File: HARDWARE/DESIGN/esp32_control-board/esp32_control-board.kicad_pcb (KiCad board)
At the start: 2 copper layers, 130 x 105 mm, 195 parts, among them J101 Power-in, J201 RFID-module1, J202 RFID-module2, J203 USB-Prog, J204 UART-Debug, J301 Lamp1, J302 Lamp2, J303 Lamp3, J304 Lamp4, J305 Lamp5, J306 Lamp6, J307 Lamp7, J308 Lamp8, J401 Lock1, J402 Lock2, J403 Lock3, J404 Lock4, J405 Lock5, J406 Lock6, J407 Lock7, J408 Lock8, Q102 DMP3013SFV-7, Q201 SS8050, Q202 SS8050, SW201 Boot, SW202 Reset, U101 LM63615DQDRRRQ1, U102 AMS1117-3.3, U201 CH343P, U202 USBLC6-2SC6, U203 ESP32-S3-WROOM-1, U204 USBLC6-2SC6, U301 MCP23008-xSS, U302 TBD62783A, U303 TBD62783A, U401 PC817, U402 PC817, U403 PC817, U404 PC817, U405 PC817, U406 PC817, U407 PC817, U408 PC817

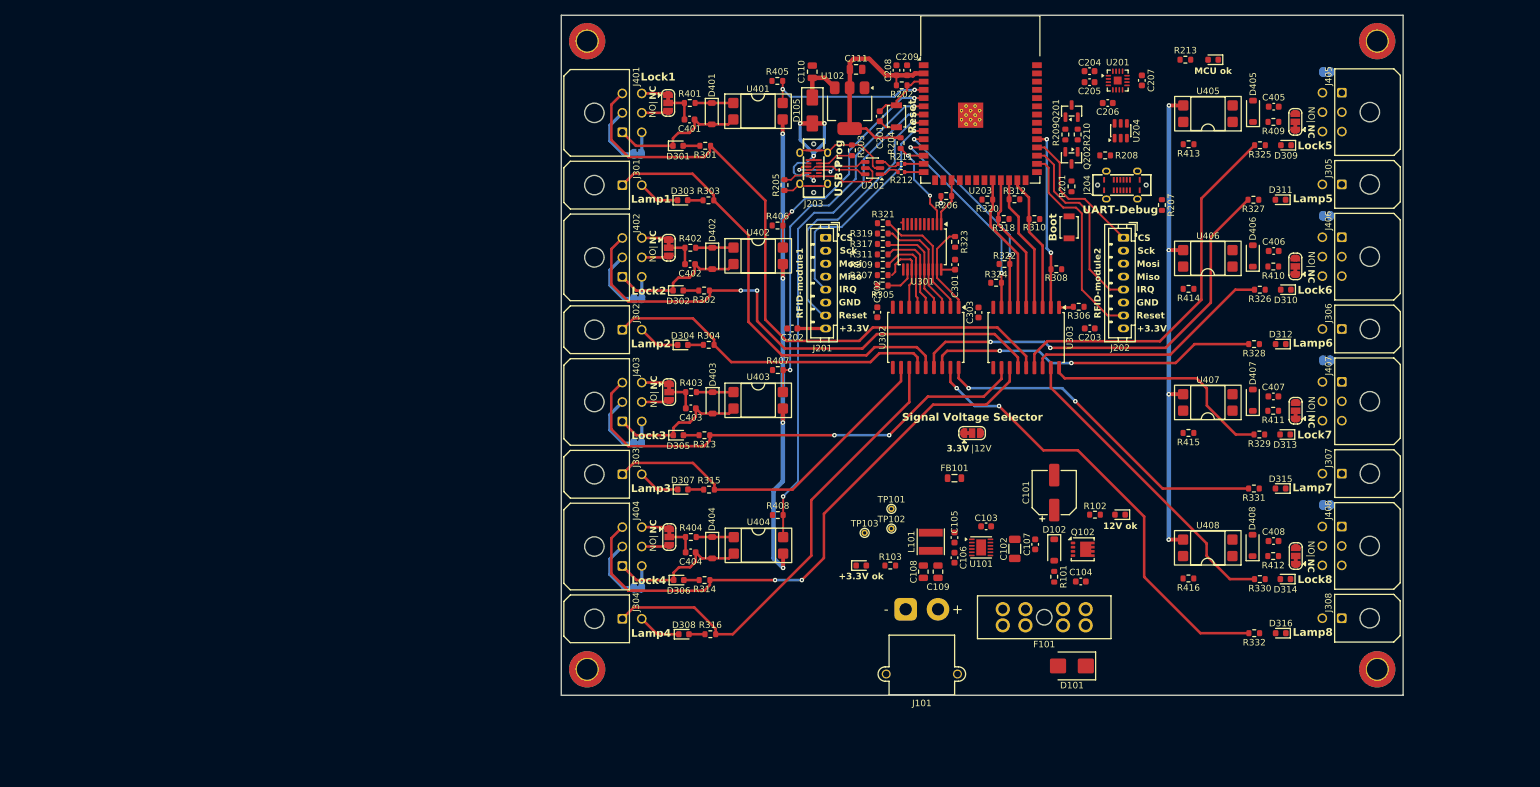
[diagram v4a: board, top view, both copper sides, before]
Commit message: 60715 - traced 75%
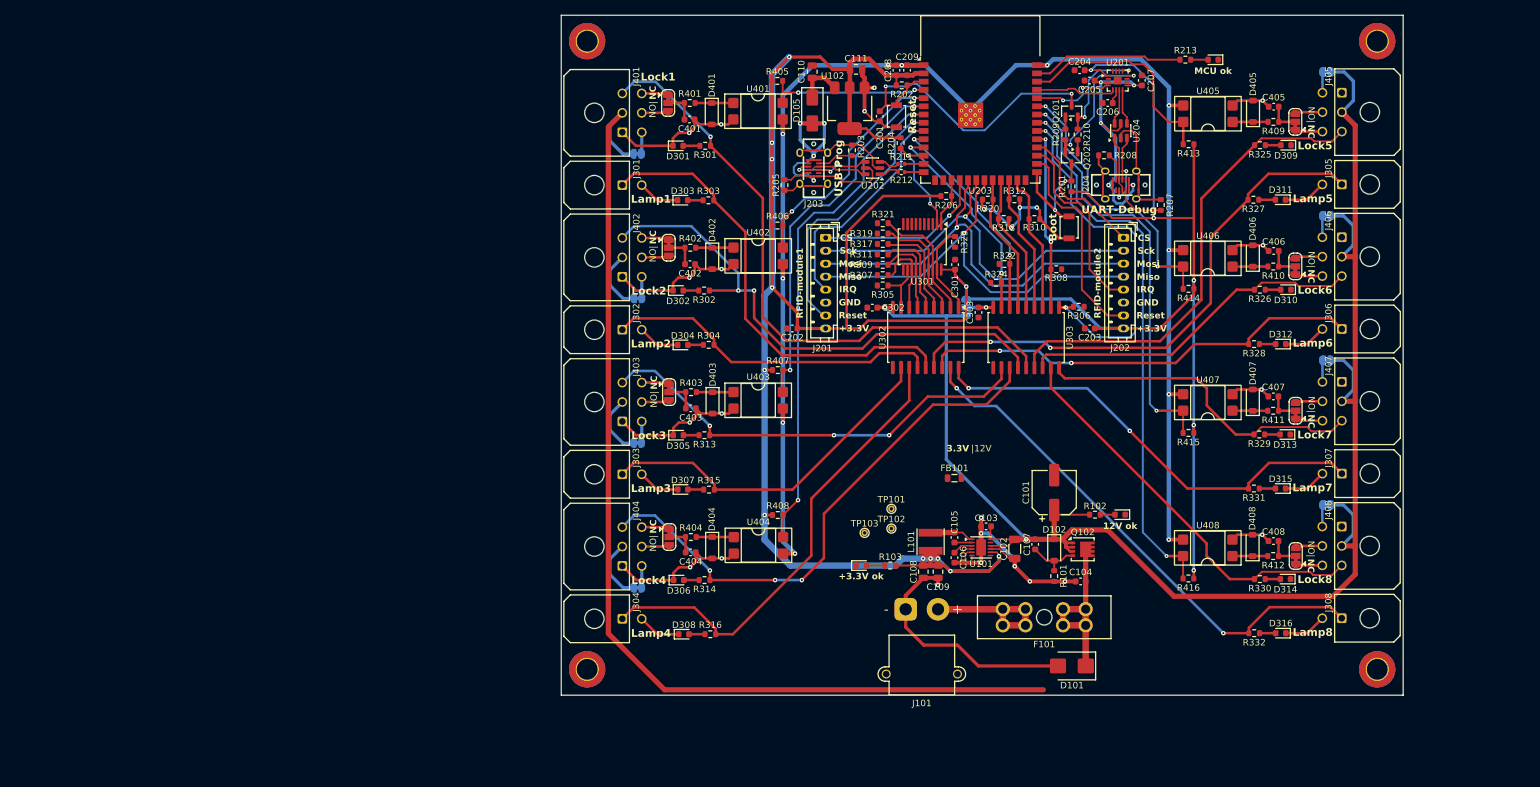
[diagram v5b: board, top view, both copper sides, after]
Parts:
- JP301: moved to B.Cu
- moved JP301 19.4 mm to (132.8, 95.0), turned to -90 degrees
- moved C204 1.54 mm to (150.3, 58.4)
- moved C302 1.05 mm to (118.3, 95.1), turned to 0 degrees
- moved C205 0.25 mm to (151.8, 60.0)
- moved J204 0.17 mm to (156.7, 76.1)
- moved R208 0.17 mm to (154.1, 71.5)
- moved R207 0.17 mm to (162.8, 79.2)
- moved R101 0.10 mm to (146.4, 136.5)
- moved R320 0.07 mm to (136.1, 78.4)
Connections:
- C208 pad 1: GND -> GND_MCU
- C209 pad 1: GND -> GND_MCU
- D201 pad 1: GND -> GND_MCU
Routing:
- net +3V3: track 40.6 -> 476.5 mm, vias 1 -> 17
- net +12V: track 38.3 -> 446.5 mm, vias 0 -> 2
- net GND: track 139.5 -> 335.4 mm, vias 0 -> 25
- net LOCK8_signal: track 0.00 -> 85.0 mm, vias 0 -> 2
- net GND_MCU: track 153.0 -> 231.2 mm, vias 8 -> 11
- net SPI_miso: track 0.00 -> 66.0 mm, vias 0 -> 1
- net SPI_mosi: track 0.00 -> 64.9 mm, vias 0 -> 1
- net LOCK7_signal: track 0.00 -> 64.7 mm, vias 0 -> 2
- net SPI_sck: track 0.00 -> 63.3 mm, vias 0 -> 1
- net LOCK1_do: track 2.25 -> 56.3 mm, vias 0 -> 2
- net Vusb: track 38.9 -> 82.8 mm, vias 4 -> 9
- net LOCK6_signal: track 0.00 -> 43.6 mm, vias 0 -> 2
- net esp_Reset: track 9.52 -> 48.4 mm, vias 0 -> 2
- net LOCK5_signal: track 0.00 -> 34.3 mm
- net +12V-fused: track 0.00 -> 27.5 mm
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
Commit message: 60825 - Schematic update and PCB-layout started
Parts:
- removed C203: 1u, Capacitor_SMD:C_0603_1608Metric
- removed C204, C205, C206, C207, C301, C302, C303: 100n, Capacitor_SMD:C_0603_1608Metric
- removed C401, C402, C403, C404, C405, C406, C407, C408: 1n, Capacitor_SMD:C_0603_1608Metric
- removed D301, D302, D305, D306, D309, D310, D313, D314: LOCK on, LED_SMD:LED_0603_1608Metric
- removed D303, D304, D307, D308, D311, D312, D315, D316: LAMP on, LED_SMD:LED_0603_1608Metric
- removed D401, D402, D403, D404, D405, D406, D407, D408: 1N4148W, Diode_SMD:D_SOD-123
- removed FB101: 80Ω@100MHz, Inductor_SMD:L_0805_2012Metric
- removed J202: RFID-module2, Connector_JST:JST_PH_B8B-PH-K_1x08_P2.00mm_Vertical
- removed J203: USB-Prog, (FOOTPRINTS):C3151749_USB_TYPE-C_Vertical
- removed J301: Lamp1, Connector_Molex:Molex_Micro-Fit_3.0_43045-0200_2x01_P3.00mm_Horizontal
- removed J302: Lamp2, Connector_Molex:Molex_Micro-Fit_3.0_43045-0200_2x01_P3.00mm_Horizontal
- removed J303: Lamp3, Connector_Molex:Molex_Micro-Fit_3.0_43045-0200_2x01_P3.00mm_Horizontal
- removed J304: Lamp4, Connector_Molex:Molex_Micro-Fit_3.0_43045-0200_2x01_P3.00mm_Horizontal
- removed J305: Lamp5, Connector_Molex:Molex_Micro-Fit_3.0_43045-0200_2x01_P3.00mm_Horizontal
- removed J306: Lamp6, Connector_Molex:Molex_Micro-Fit_3.0_43045-0200_2x01_P3.00mm_Horizontal
- removed J307: Lamp7, Connector_Molex:Molex_Micro-Fit_3.0_43045-0200_2x01_P3.00mm_Horizontal
- removed J308: Lamp8, Connector_Molex:Molex_Micro-Fit_3.0_43045-0200_2x01_P3.00mm_Horizontal
- removed J404: Lock4, Connector_Molex:Molex_Micro-Fit_3.0_43045-0600_2x03_P3.00mm_Horizontal
- removed JP301: Signal Voltage Selector, Jumper:SolderJumper-3_P1.3mm_Bridged12_RoundedPad1.0x1.5mm
- removed JP401, JP402, JP403, JP404, JP405, JP406, JP407, JP408: Switch State Selector, Jumper:SolderJumper-3_P1.3mm_Bridged12_RoundedPad1.0x1.5mm
- removed JP409, JP410, JP411, JP412, JP413, JP414, JP415, JP416: 12V-to-COM, Jumper:SolderJumper-2_P1.3mm_Bridged_RoundedPad1.0x1.5mm
- removed Q201, Q202: SS8050, Package_TO_SOT_SMD:SOT-23
- removed R101, R201, R202, R209, R210, R305, R306, R307, R308, R309, R310, R311, R312, R317, R318, R319, R320, R321, R322, R323, R324: 12k, Resistor_SMD:R_0603_1608Metric
- removed R203, R205, R301, R302, R303, R304, R313, R314, R315, R316, R325, R326, R327, R328, R329, R330, R331, R332: 5k1, Resistor_SMD:R_0603_1608Metric
- removed R401, R402, R403, R404, R409, R410, R411, R412: 1k2, Resistor_SMD:R_0603_1608Metric
- removed R405, R406, R407, R408, R413, R414, R415, R416: 10k, Resistor_SMD:R_0603_1608Metric
- removed U201: CH343P, Package_DFN_QFN:TQFN-16-1EP_3x3mm_P0.5mm_EP1.23x1.23mm
- removed U202: USBLC6-2SC6, Package_TO_SOT_SMD:SOT-23-6
- removed U301: MCP23008-xSS, Package_SO:SSOP-20_5.3x7.2mm_P0.65mm
- removed U302, U303: TBD62783A, Package_SO:SOIC-18W_7.5x11.6mm_P1.27mm
- removed U401, U402, U403, U404, U405, U406, U407, U408: PC817, Package_DIP:DIP-4_W7.62mm_SMDSocket_SmallPads
- added C210: 100n, Capacitor_SMD:C_0603_1608Metric, F.Cu at (48.5, 125.7)
- added C211: 100n, Capacitor_SMD:C_0603_1608Metric, F.Cu at (-3.02, 130.4)
- added C212: 10n, Capacitor_SMD:C_0603_1608Metric, F.Cu at (-3.02, 132.9)
- added C213: 10n, Capacitor_SMD:C_0603_1608Metric, F.Cu at (-3.02, 135.5)
- added C214: 10n, Capacitor_SMD:C_0603_1608Metric, F.Cu at (-3.02, 138.0)
- added C215: 10n, Capacitor_SMD:C_0603_1608Metric, F.Cu at (-3.02, 140.5)
- added C216: 100n, Capacitor_SMD:C_0603_1608Metric, F.Cu at (28.0, 150.7)
- added C217: 1u, Capacitor_SMD:C_0603_1608Metric, F.Cu at (48.5, 128.2)
- added C218: 4u7, Capacitor_SMD:C_0805_2012Metric, F.Cu at (13.2, 154.8)
- added C219: 4u7, Capacitor_SMD:C_0805_2012Metric, F.Cu at (13.2, 157.8)
- added C220: 10n, Capacitor_SMD:C_0603_1608Metric, F.Cu at (-3.02, 143.0)
- added C221: 10n, Capacitor_SMD:C_0603_1608Metric, F.Cu at (-3.02, 145.5)
- added C409: 1n, Capacitor_SMD:C_0603_1608Metric, F.Cu at (13.9, 105.8)
- added C410: 1n, Capacitor_SMD:C_0603_1608Metric, F.Cu at (13.9, 108.4)
- added C411: 1n, Capacitor_SMD:C_0603_1608Metric, F.Cu at (13.9, 110.9)
- added C412: 1n, Capacitor_SMD:C_0603_1608Metric, F.Cu at (13.9, 113.4)
- added D106: XL-1608UOC-06, LED_SMD:LED_0603_1608Metric, F.Cu at (2.28, 110.6)
- added D107: XL-1608UOC-06, LED_SMD:LED_0603_1608Metric, F.Cu at (2.28, 113.2)
- added D108: XL-1608UOC-06, LED_SMD:LED_0603_1608Metric, F.Cu at (2.28, 115.8)
- added D109: XL-1608UOC-06, LED_SMD:LED_0603_1608Metric, F.Cu at (2.28, 118.4)
- added D112: XL-1608UWC-04, LED_SMD:LED_0603_1608Metric, F.Cu at (8.97, 154.6)
- added D113: XL-1608UWC-04, LED_SMD:LED_0603_1608Metric, F.Cu at (8.97, 157.2)
- added D114: XL-1608UWC-04, LED_SMD:LED_0603_1608Metric, F.Cu at (8.97, 159.8)
- added D115: XL-1608UWC-04, LED_SMD:LED_0603_1608Metric, F.Cu at (8.97, 162.4)
- added D202: MCU ok, LED_SMD:LED_0603_1608Metric, F.Cu at (48.6, 135.8)
- added D203: XL-1608UBC-06A, LED_SMD:LED_0603_1608Metric, F.Cu at (48.6, 138.4)
- added D204: XL-1608SURUGC, LED_SMD:LED_0603_1608Metric, F.Cu at (48.6, 141.0)
- added D317: LAMP on, LED_SMD:LED_0603_1608Metric, F.Cu at (8.97, 165.0)
- added D409: 1N4148W, Diode_SMD:D_SOD-123, F.Cu at (19.8, 84.0)
- added D410: 1N4148W, Diode_SMD:D_SOD-123, F.Cu at (19.8, 87.4)
- added D411: 1N4148W, Diode_SMD:D_SOD-123, F.Cu at (19.8, 90.7)
- added D412: 1N4148W, Diode_SMD:D_SOD-123, F.Cu at (19.8, 94.1)
- added D5: PESD1CAN, Package_TO_SOT_SMD:SOT-23, F.Cu at (37.6, 165.4)
- added J309: Lamp1, Connector_Molex:Molex_Micro-Fit_3.0_43045-0200_2x01_P3.00mm_Horizontal, F.Cu at (11.6, 136.6)
- added J4: Termination, Connector_PinHeader_2.54mm:PinHeader_1x02_P2.54mm_Horizontal, F.Cu at (87.0, 61.4)
- added J409: Lock1, Connector_Molex:Molex_Micro-Fit_3.0_43045-0600_2x03_P3.00mm_Horizontal, F.Cu at (115.2, 145.9)
- added J410: Lock2, Connector_Molex:Molex_Micro-Fit_3.0_43045-0600_2x03_P3.00mm_Horizontal, F.Cu at (130.8, 145.8)
- added J411: B3B-PH-K-S(LF)(SN), Connector_JST:JST_PH_B3B-PH-K_1x03_P2.00mm_Vertical, F.Cu at (-12.0, 155.6)
- added J412: B3B-PH-K-S(LF)(SN), Connector_JST:JST_PH_B3B-PH-K_1x03_P2.00mm_Vertical, F.Cu at (-12.0, 162.2)
- added Q401: AO3401A, Package_TO_SOT_SMD:SOT-23, F.Cu at (14.4, 84.6)
- added Q402: BSS138, Package_TO_SOT_SMD:SOT-23, F.Cu at (14.4, 89.0)
- added Q403: BSS138, Package_TO_SOT_SMD:SOT-23, F.Cu at (14.4, 93.5)
- added Q404: AO3401A, Package_TO_SOT_SMD:SOT-23, F.Cu at (14.4, 97.9)
- added Q405: BSS138, Package_TO_SOT_SMD:SOT-23, F.Cu at (14.4, 102.4)
- added Q406: DMP6180SK3-13, Package_TO_SOT_SMD:TO-252-2, F.Cu at (-8.06, 116.0)
- added R105: 12k, Resistor_SMD:R_0603_1608Metric, F.Cu at (13.9, 115.9)
- added R106: 27k, Resistor_SMD:R_0603_1608Metric, F.Cu at (13.9, 118.4)
- added R107: 12k, Resistor_SMD:R_0603_1608Metric, F.Cu at (13.9, 120.9)
- added R108: 12k, Resistor_SMD:R_0603_1608Metric, F.Cu at (28.0, 109.2)
- added R109: 12k, Resistor_SMD:R_0603_1608Metric, F.Cu at (48.5, 130.7)
- added R110: 12k, Resistor_SMD:R_0603_1608Metric, F.Cu at (52.5, 120.7)
- added R111: 120, Resistor_SMD:R_0603_1608Metric, F.Cu at (13.9, 123.4)
- added R112: 120, Resistor_SMD:R_0603_1608Metric, F.Cu at (18.0, 105.8)
- added R113: 12k, Resistor_SMD:R_0603_1608Metric, F.Cu at (18.0, 108.4)
- added R114: 27k, Resistor_SMD:R_0603_1608Metric, F.Cu at (18.0, 110.9)
- added R115: 12k, Resistor_SMD:R_0603_1608Metric, F.Cu at (18.0, 113.4)
- added R116: 12k, Resistor_SMD:R_0603_1608Metric, F.Cu at (18.0, 115.9)
- added R117: 12k, Resistor_SMD:R_0603_1608Metric, F.Cu at (18.0, 118.4)
- added R118: 12k, Resistor_SMD:R_0603_1608Metric, F.Cu at (18.0, 120.9)
- added R119: 12k, Resistor_SMD:R_0603_1608Metric, F.Cu at (18.0, 123.4)
- added R120: 1M, Resistor_SMD:R_0603_1608Metric, F.Cu at (52.5, 123.2)
- added R121: 270k, Resistor_SMD:R_0603_1608Metric, F.Cu at (52.5, 125.7)
- added R122: 120, Resistor_SMD:R_0603_1608Metric, F.Cu at (28.0, 153.2)
- added R123: 12k, Resistor_SMD:R_0603_1608Metric, F.Cu at (28.0, 155.7)
- added R124: 120, Resistor_SMD:R_0603_1608Metric, F.Cu at (22.0, 105.8)
- added R125: 12k, Resistor_SMD:R_0603_1608Metric, F.Cu at (0.99, 127.9)
- added R126: 120, Resistor_SMD:R_0603_1608Metric, F.Cu at (0.99, 130.4)
- added R127: 12k, Resistor_SMD:R_0603_1608Metric, F.Cu at (0.99, 132.9)
- added R128: 120, Resistor_SMD:R_0603_1608Metric, F.Cu at (0.99, 135.5)
- added R129: 12k, Resistor_SMD:R_0603_1608Metric, F.Cu at (0.99, 138.0)
- added R130: 12k, Resistor_SMD:R_0603_1608Metric, F.Cu at (0.99, 140.5)
- added R131: 120, Resistor_SMD:R_0603_1608Metric, F.Cu at (0.99, 143.0)
- added R132: 120, Resistor_SMD:R_0603_1608Metric, F.Cu at (0.99, 145.5)
- added R133: 12k, Resistor_SMD:R_0603_1608Metric, F.Cu at (22.0, 108.4)
- added R134: 12k, Resistor_SMD:R_0603_1608Metric, F.Cu at (22.0, 110.9)
- added R214: 1k, Resistor_SMD:R_0603_1608Metric, F.Cu at (56.5, 128.2)
- added R215: 0R, Resistor_SMD:R_0402_1005Metric, F.Cu at (57.2, 108.6)
- added R333: 5k1, Resistor_SMD:R_0603_1608Metric, F.Cu at (5.00, 127.9)
- added R417: 1k, Resistor_SMD:R_0603_1608Metric, F.Cu at (22.0, 113.4)
- added R419: 1k, Resistor_SMD:R_0603_1608Metric, F.Cu at (22.0, 115.9)
- added R420: 1k, Resistor_SMD:R_0603_1608Metric, F.Cu at (22.0, 118.4)
- added R421: 1k, Resistor_SMD:R_0603_1608Metric, F.Cu at (22.0, 120.9)
- added R422: 1k, Resistor_SMD:R_0603_1608Metric, F.Cu at (5.00, 130.4)
- added R423: 1k, Resistor_SMD:R_0603_1608Metric, F.Cu at (5.00, 132.9)
- added R424: 1k, Resistor_SMD:R_0603_1608Metric, F.Cu at (5.00, 135.5)
- added R425: 1k, Resistor_SMD:R_0603_1608Metric, F.Cu at (5.00, 138.0)
- added R426: 1k, Resistor_SMD:R_0603_1608Metric, F.Cu at (5.00, 140.5)
- added R427: 1k, Resistor_SMD:R_0603_1608Metric, F.Cu at (5.00, 143.0)
- added U205: USBLC6-2SC6, Package_TO_SOT_SMD:SOT-23-6, F.Cu at (13.6, 161.7)
- added U409: PC817, Package_DIP:DIP-4_W7.62mm_SMDSocket_SmallPads, F.Cu at (6.09, 85.7)
- added U410: PC817, Package_DIP:DIP-4_W7.62mm_SMDSocket_SmallPads, F.Cu at (6.09, 92.5)
- added U411: PC817, Package_DIP:DIP-4_W7.62mm_SMDSocket_SmallPads, F.Cu at (6.09, 99.2)
- added U412: PC817, Package_DIP:DIP-4_W7.62mm_SMDSocket_SmallPads, F.Cu at (6.09, 106.0)
- added U6: TCAN330, Package_TO_SOT_SMD:SOT-23-8, F.Cu at (32.6, 165.5)
- C208: value 1u -> 22u; footprint Capacitor_SMD:C_0603_1608Metric -> Capacitor_SMD:C_0805_2012Metric
- J204: value UART-Debug -> USB-prog
- J401: value Lock1 -> B3B-PH-K-K(LF)(SN); footprint Connector_Molex:Molex_Micro-Fit_3.0_43045-0600_2x03_P3.00mm_Horizontal -> Connector_JST:JST_PH_B3B-PH-K_1x03_P2.00mm_Vertical
- J402: value Lock2 -> B4B-PH-K-S(LF)(SN); footprint Connector_Molex:Molex_Micro-Fit_3.0_43045-0600_2x03_P3.00mm_Horizontal -> Connector_JST:JST_PH_B4B-PH-K_1x04_P2.00mm_Vertical
- J403: value Lock3 -> B4B-PH-K-S(LF)(SN); footprint Connector_Molex:Molex_Micro-Fit_3.0_43045-0600_2x03_P3.00mm_Horizontal -> Connector_JST:JST_PH_B4B-PH-K_1x04_P2.00mm_Vertical
- J405: value Lock5 -> B3B-PH-K-S(LF)(SN); footprint Connector_Molex:Molex_Micro-Fit_3.0_43045-0600_2x03_P3.00mm_Horizontal -> Connector_JST:JST_PH_B3B-PH-K_1x03_P2.00mm_Vertical
- J406: value Lock6 -> B3B-PH-K-S(LF)(SN); footprint Connector_Molex:Molex_Micro-Fit_3.0_43045-0600_2x03_P3.00mm_Horizontal -> Connector_JST:JST_PH_B3B-PH-K_1x03_P2.00mm_Vertical
- J407: value Lock7 -> B3B-PH-K-S(LF)(SN); footprint Connector_Molex:Molex_Micro-Fit_3.0_43045-0600_2x03_P3.00mm_Horizontal -> Connector_JST:JST_PH_B3B-PH-K_1x03_P2.00mm_Vertical
- J408: value Lock8 -> B3B-PH-K-S(LF)(SN); footprint Connector_Molex:Molex_Micro-Fit_3.0_43045-0600_2x03_P3.00mm_Horizontal -> Connector_JST:JST_PH_B3B-PH-K_1x03_P2.00mm_Vertical
- U203: value ESP32-S3-WROOM-1 -> ESP32-S3-WROOM-1U; footprint RF_Module:ESP32-S3-WROOM-1 -> RF_Module:ESP32-S3-WROOM-1U
- moved J405 213.7 mm to (-12.0, 129.4), turned to 0 degrees
- moved J406 209.3 mm to (-12.0, 135.9), turned to 0 degrees
- moved J407 206.0 mm to (-12.0, 142.5), turned to 0 degrees
- moved J408 203.8 mm to (-12.0, 149.1), turned to 0 degrees
- moved D201 144.3 mm to (48.6, 133.2), turned to 0 degrees
- moved R213 129.9 mm to (56.5, 125.7)
- moved C104 129.9 mm to (28.0, 94.2)
- moved R102 126.8 mm to (28.0, 104.2), turned to 0 degrees
- moved C107 119.3 mm to (28.0, 101.7), turned to 0 degrees
- moved C103 114.1 mm to (28.0, 91.7), turned to 0 degrees
- moved R207 114.1 mm to (56.5, 120.7), turned to 0 degrees
- moved C202 112.9 mm to (-3.02, 127.9), turned to 0 degrees
- moved R208 110.3 mm to (56.5, 123.2)
- moved C208 108.6 mm to (52.8, 142.2), turned to 0 degrees
- moved C106 108.6 mm to (28.0, 99.2), turned to 0 degrees
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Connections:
- net esp_LED renamed esp_LED_green
- J204 pad A6: espS_USB_dp -> esp_USB_dP
- J204 pad A7: espS_USB_dm -> esp_USB_dN
- J204 pad B6: espS_USB_dp -> esp_USB_dP
- J204 pad B7: espS_USB_dm -> esp_USB_dN
- J401 pad 1: GND -> CAN+_conn.
- J401 pad 2: +12V -> CAN-_conn.
- J401 pad 3: LOCK1_ctrl -> GND
- J402 pad 1: GND -> +3V3
- J402 pad 2: +12V -> GND
- J402 pad 3: LOCK2_ctrl -> I2C_sda
- J402 pad 4: SWITCH2-COM -> I2C_scl
- J403 pad 1: GND -> +3V3
- J403 pad 2: +12V -> GND
- J403 pad 3: LOCK3_ctrl -> esp_TXD
- J403 pad 4: SWITCH3-COM -> esp_RXD
- J405 pad 1: GND -> +3V3
- J405 pad 2: +12V -> GND
- J405 pad 3: LOCK5_ctrl -> di_SENSOR_ext1
- J406 pad 1: GND -> +3V3
- J406 pad 2: +12V -> GND
- J406 pad 3: LOCK6_ctrl -> di_SENSOR_ext2
- J407 pad 1: GND -> +3V3
- J407 pad 2: +12V -> GND
- J407 pad 3: LOCK7_ctrl -> di_SENSOR_ext3
- J408 pad 1: GND -> +3V3
- J408 pad 2: +12V -> GND
- J408 pad 3: LOCK8_ctrl -> di_SENSOR_ext4
- R211 pad 1: espU_USB_d- -> esp_USB_d-
- R212 pad 1: espU_USB_d+ -> esp_USB_d+
- U203 pad 10: LOCK7_do -> unconnected-(U203-IO17-Pad10)
- U203 pad 11: LOCK8_do -> unconnected-(U203-IO18-Pad11)
- U203 pad 22: LOCK6_do -> unconnected-(U203-IO14-Pad22)
- U203 pad 23: LOCK5_do -> unconnected-(U203-IO21-Pad23)
- U203 pad 24: LOCK4_do -> unconnected-(U203-IO47-Pad24)
- U203 pad 25: LOCK3_do -> unconnected-(U203-IO48-Pad25)
- U203 pad 28: RFID2_reset -> unconnected-(U203-IO35-Pad28)
- U203 pad 29: RFID2_irq -> unconnected-(U203-IO36-Pad29)
- U203 pad 30: SPI_cs2 -> unconnected-(U203-IO37-Pad30)
- U203 pad 31: LOCK2_do -> unconnected-(U203-IO38-Pad31)
- U203 pad 32: LOCK1_do -> unconnected-(U203-IO39-Pad32)
- U203 pad 33: LOCK8_signal -> unconnected-(U203-IO40-Pad33)
- U203 pad 34: LOCK7_signal -> unconnected-(U203-IO41-Pad34)
- U203 pad 35: LOCK6_signal -> unconnected-(U203-IO42-Pad35)
- U203 pad 38: LOCK5_signal -> unconnected-(U203-IO2-Pad38)
- U203 pad 4: LOCK1_signal -> TWAI_TX
- U203 pad 5: LOCK2_signal -> TWAI_RX
- U203 pad 6: LOCK3_signal -> esp_ADC1_ch5
- U203 pad 7: LOCK4_signal -> esp_ADC1_ch6
- U204 pad 1: espS_USB_dp -> esp_USB_dN
- U204 pad 3: espS_USB_dm -> esp_USB_dP
- U204 pad 4: espS_USB_d- -> esp_USB_d+
- U204 pad 6: espS_USB_d+ -> esp_USB_d-
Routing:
- net +3V3: track 476.5 -> 0.00 mm, vias 17 -> 0
- net +12V: track 446.5 -> 0.00 mm, vias 2 -> 0
- net GND: track 335.4 -> 0.00 mm, vias 25 -> 0
- net GND_MCU: track 231.2 -> 0.00 mm, vias 11 -> 0
- net LOCK1_ctrl: track 95.7 -> 0.00 mm, vias 1 -> 0
- net LOCK8_signal: track 85.0 -> 0.00 mm, vias 2 -> 0
- net LAMP5: track 84.6 -> 0.00 mm, vias 2 -> 0
- net LOCK4_ctrl: track 84.4 -> 0.00 mm, vias 3 -> 0
- net Vusb: track 82.8 -> 0.00 mm, vias 9 -> 0
- net LOCK2_ctrl: track 82.2 -> 0.00 mm, vias 2 -> 0
- net LAMP8: track 81.6 -> 0.00 mm, vias 2 -> 0
- net LOCK4_signal: track 77.3 -> 0.00 mm, vias 2 -> 0
- net LOCK5_ctrl: track 73.4 -> 0.00 mm
- net LAMP4: track 72.5 -> 0.00 mm
- net LAMP7: track 70.7 -> 0.00 mm, vias 2 -> 0
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
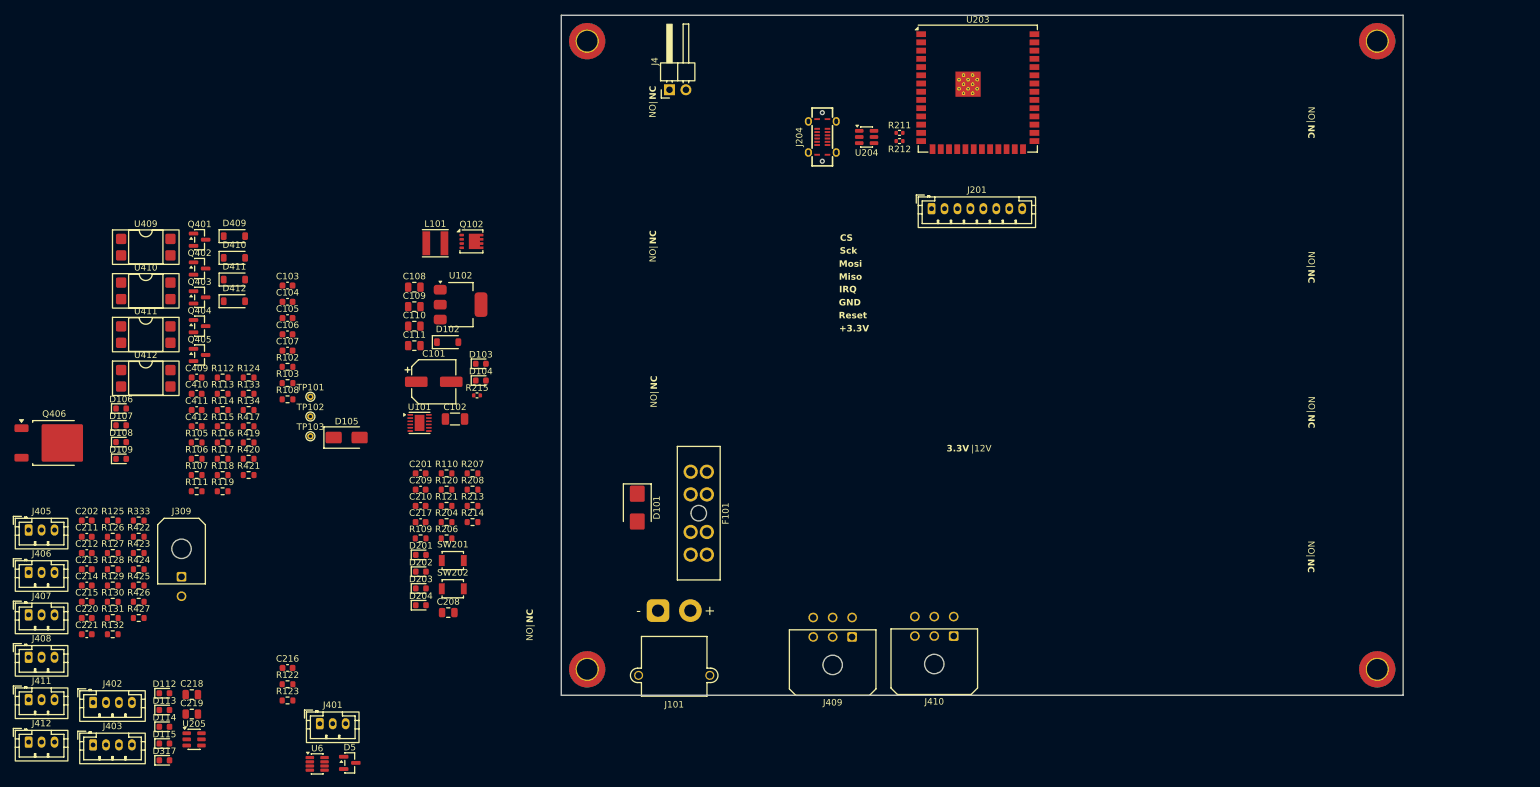
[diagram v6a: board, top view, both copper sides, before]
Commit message: 60828 - Schematic updated, preliminary PCB-layout done
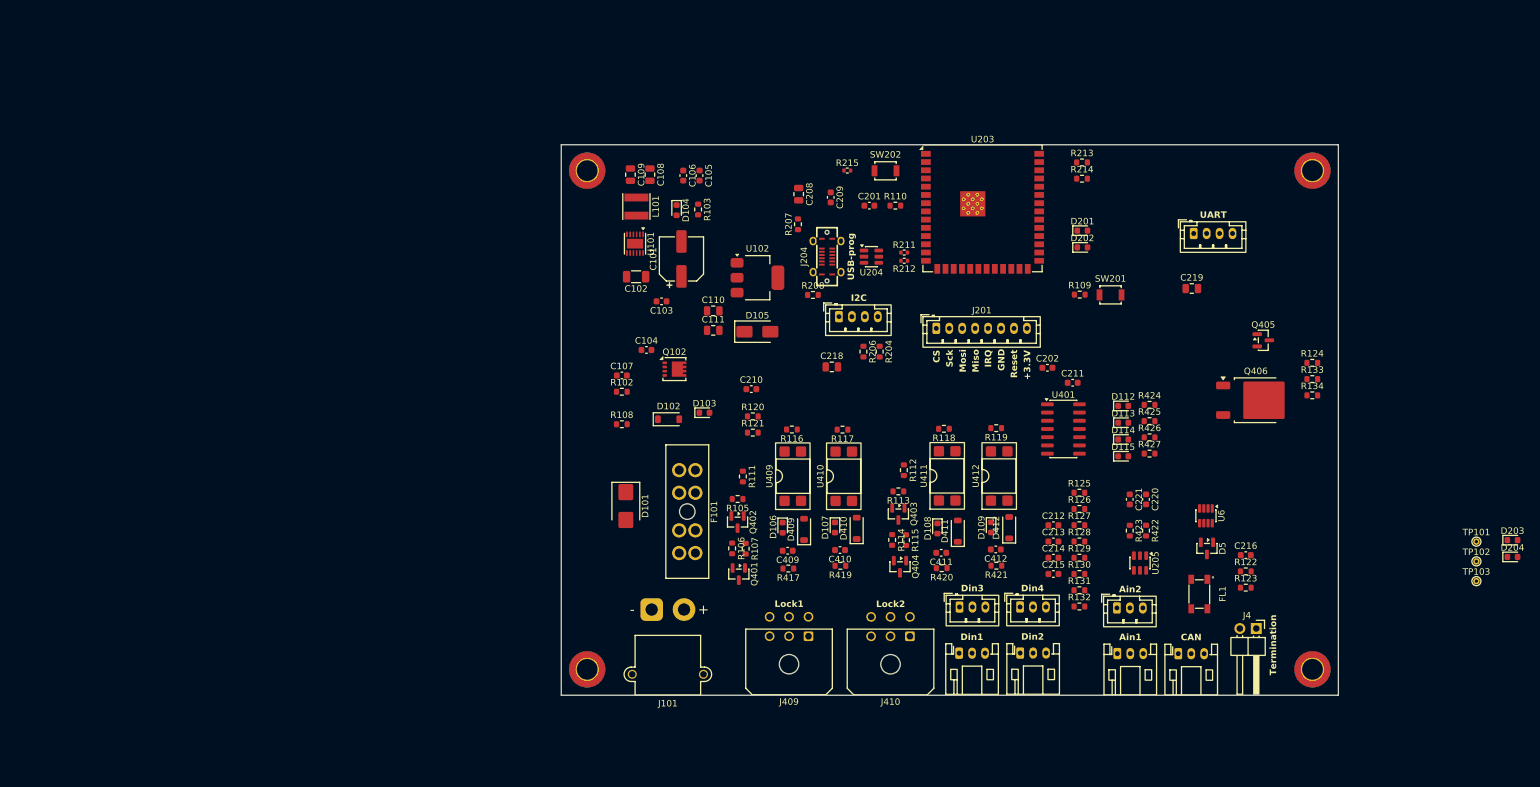
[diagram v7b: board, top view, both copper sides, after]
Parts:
- removed C217: 1u, Capacitor_SMD:C_0603_1608Metric
- removed D317: LAMP on, LED_SMD:LED_0603_1608Metric
- removed J309: Lamp1, Connector_Molex:Molex_Micro-Fit_3.0_43045-0200_2x01_P3.00mm_Horizontal
- removed R333: 5k1, Resistor_SMD:R_0603_1608Metric
- added FL1: Common Mode Choke, (FOOTPRINTS):C76584_IND-SMD_4P-L4.5-W3.2-TL, F.Cu at (168.8, 139.3)
- added U401: SN74LVC125ADR, Package_SO:SOIC-14_3.9x8.7mm_P1.27mm, F.Cu at (147.8, 113.8)
- J401: value B3B-PH-K-K(LF)(SN) -> CAN; footprint Connector_JST:JST_PH_B3B-PH-K_1x03_P2.00mm_Vertical -> Connector_JST:JST_PH_S3B-PH-K_1x03_P2.00mm_Horizontal
- J402: value B4B-PH-K-S(LF)(SN) -> I2C
- J403: value B4B-PH-K-S(LF)(SN) -> UART
- J405: value B3B-PH-K-S(LF)(SN) -> Din1; footprint Connector_JST:JST_PH_B3B-PH-K_1x03_P2.00mm_Vertical -> Connector_JST:JST_PH_S3B-PH-K_1x03_P2.00mm_Horizontal
- J406: value B3B-PH-K-S(LF)(SN) -> Din3
- J407: value B3B-PH-K-S(LF)(SN) -> Din2; footprint Connector_JST:JST_PH_B3B-PH-K_1x03_P2.00mm_Vertical -> Connector_JST:JST_PH_S3B-PH-K_1x03_P2.00mm_Horizontal
- J408: value B3B-PH-K-S(LF)(SN) -> Din4
- J411: value B3B-PH-K-S(LF)(SN) -> Ain2
- J412: value B3B-PH-K-S(LF)(SN) -> Ain1; footprint Connector_JST:JST_PH_B3B-PH-K_1x03_P2.00mm_Vertical -> Connector_JST:JST_PH_S3B-PH-K_1x03_P2.00mm_Horizontal
- moved J403 187.4 mm to (167.9, 83.6)
- moved Q406 185.7 mm to (177.5, 109.4)
- moved TP101 181.4 mm to (211.6, 131.2)
- moved TP102 181.4 mm to (211.6, 134.2)
- moved TP103 181.4 mm to (211.6, 137.3)
- moved D203 168.7 mm to (217.1, 131.0)
- moved D204 168.7 mm to (217.1, 133.6)
- moved J412 168.7 mm to (156.1, 148.5)
- moved J411 168.7 mm to (156.1, 141.4)
- moved C219 167.8 mm to (167.6, 92.1)
- moved C220 164.6 mm to (160.5, 124.7), turned to -90 degrees
- moved Q405 164.3 mm to (178.7, 100.1)
- moved R124 164.3 mm to (186.2, 103.6)
- moved R133 164.3 mm to (186.2, 106.1)
- moved R134 164.3 mm to (186.2, 108.6)
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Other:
- board size 130 x 105 mm -> 120 x 85 mm
- board text removed: "3.3V"
- board text removed: "NC"
- board text removed: "NO|"
- board text removed: "|12V"
